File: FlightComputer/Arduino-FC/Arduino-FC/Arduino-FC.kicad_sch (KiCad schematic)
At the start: 23 parts, among them J1 Conn_01x04, J2 Conn_01x08, J3 Conn_01x06, J4 Conn_01x03, J5 Screw_Terminal_01x02, U1 NRF24L01_Breakout

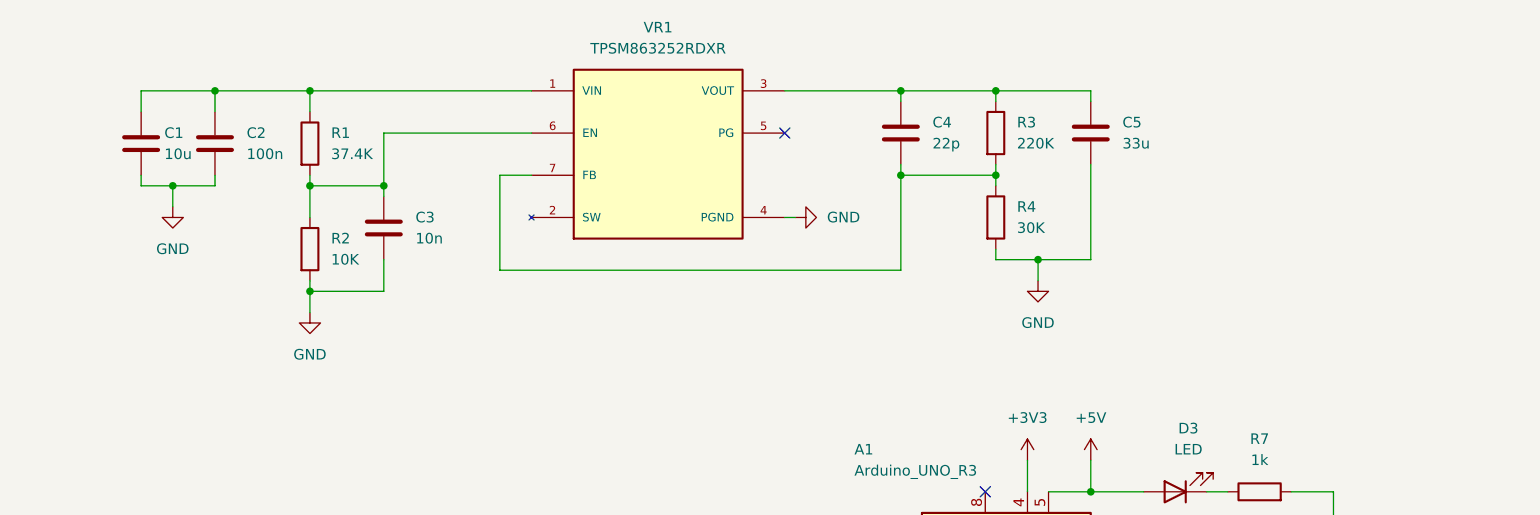
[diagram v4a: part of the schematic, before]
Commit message: Added switch
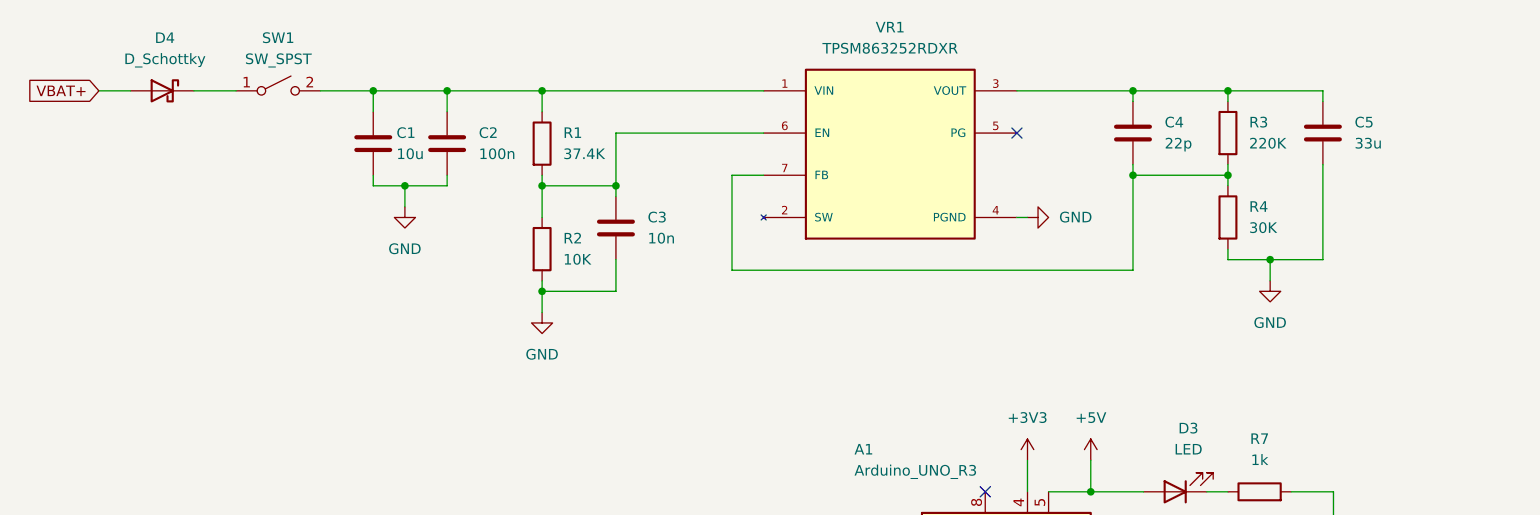
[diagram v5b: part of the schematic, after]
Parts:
- added D4: D_Schottky, Diode_SMD:D_0201_0603Metric_Pad0.64x0.40mm_HandSolder, symbol Device:D_Schottky
- added SW1: SW_SPST, Button_Switch_THT:SW_DIP_SPSTx01_Slide_6.7x4.1mm_W7.62mm_P2.54mm_LowProfile, symbol Switch:SW_SPST
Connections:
- net VBAT+: now also D4.2 (A)
- net at C1.1, C2.1, R1.1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: now also SW1.2 (B)
- new net: D4.1 (K), SW1.1 (A)
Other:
- moved on the sheet: C1, C2, C3, C4, C5, R1, R2, R3, R4, VR1

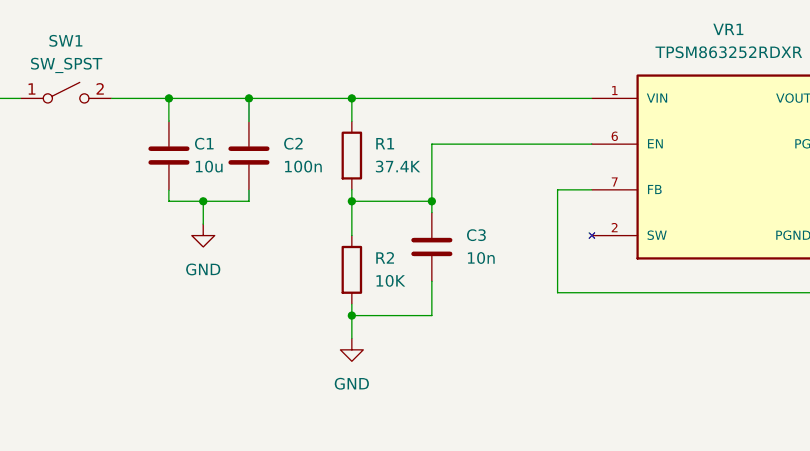
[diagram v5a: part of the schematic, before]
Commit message: updated resistor val
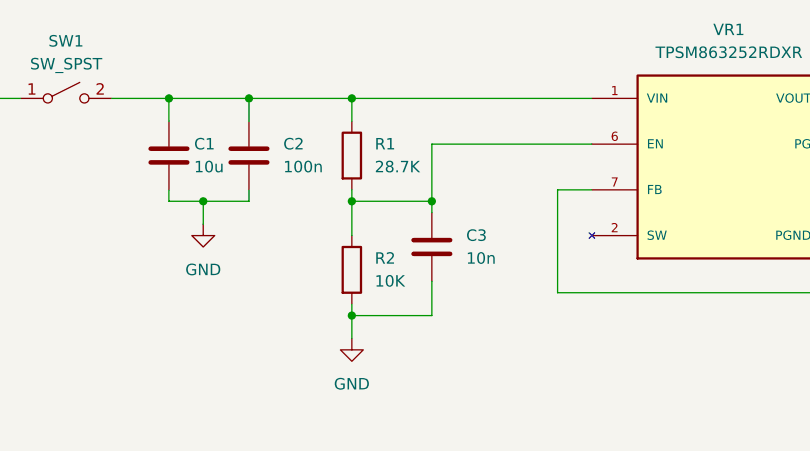
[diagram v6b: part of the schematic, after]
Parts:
- R1: value 37.4K -> 28.7K
